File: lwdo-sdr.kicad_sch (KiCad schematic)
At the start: 21 parts, among them J101 IN1, J102 IN2, J103 IN3, J104 IN4, J105 USB_B, J106 CLK_OUT, J107 REF_IN

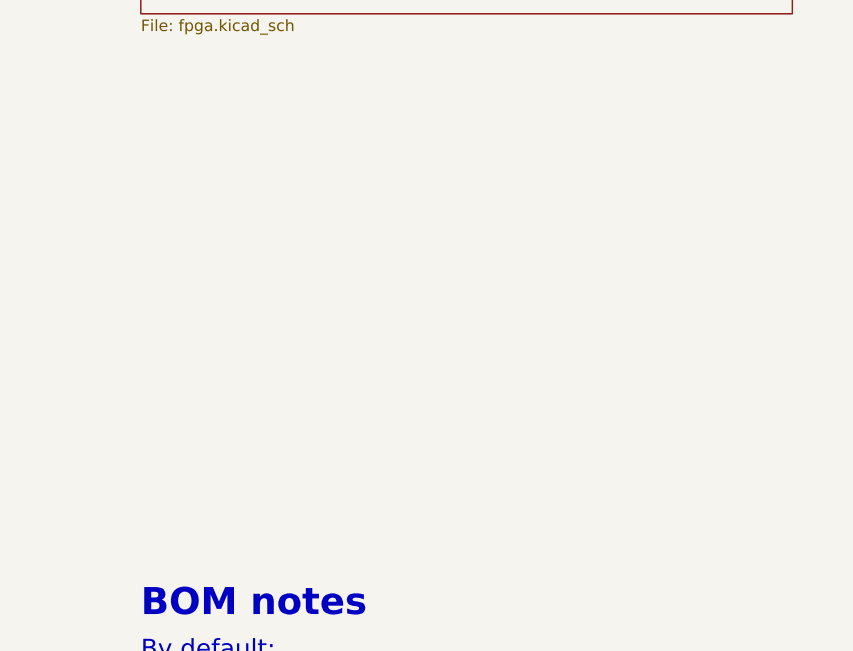
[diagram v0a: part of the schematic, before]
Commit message: Schematic: add mounting holes
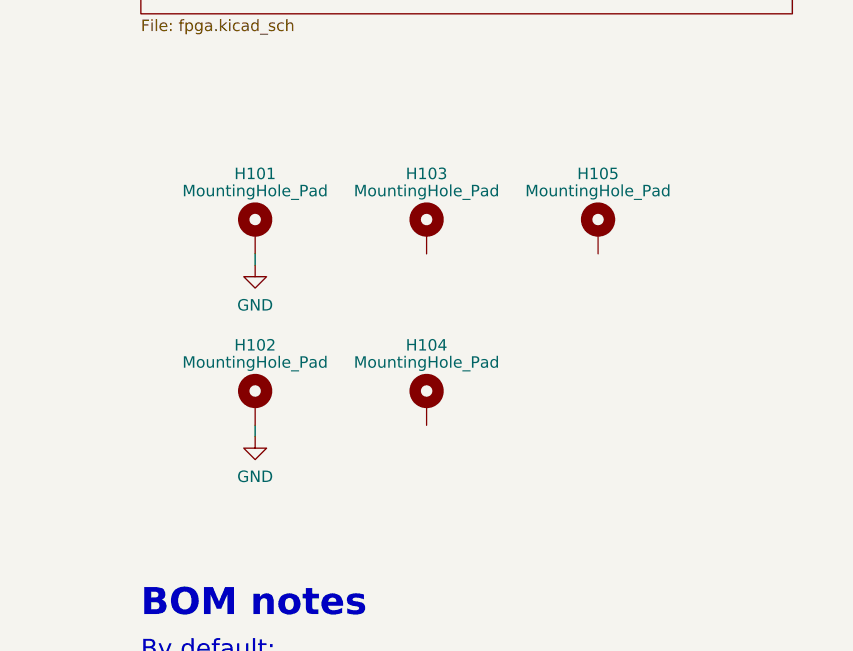
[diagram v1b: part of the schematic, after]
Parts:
- added H101, H102, H103, H104, H105: MountingHole_Pad, MountingHole:MountingHole_3.2mm_M3_Pad, symbol Mechanical:MountingHole_Pad
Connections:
- net GND: now also H101.1, H102.1
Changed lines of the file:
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@@
+    (stroke (width 0) (type default) (color 0 0 0 0))
+  )
+  (wire (pts (xy 215.9 187.96) (xy 215.9 189.23))
     (stroke (width 0) (type default) (color 0 0 0 0))
   )
@@
   )
   (wire (pts (xy 121.92 125.73) (xy 121.92 107.95))
+    (stroke (width 0) (type default) (color 0 0 0 0))
+  )
+  (wire (pts (xy 215.9 168.91) (xy 215.9 170.18))
     (stroke (width 0) (type default) (color 0 0 0 0))
   )
@@
     )
     (property "Datasheet" "" (id 3) (at 63.5 82.55 0)
+      (effects (font (size 1.27 1.27)) hide)
+    )
+    (pin "1")
+  )
+  (symbol (lib_id "Mechanical:MountingHole_Pad") (at 234.95 185.42 0) (unit 1)
+    (in_bom yes) (on_board yes) (fields_autoplaced)
+    (property "Reference" "H104" (id 0) (at 234.95 179.07 0))
+    (property "Value" "MountingHole_Pad" (id 1) (at 234.95 180.975 0))
+    (property "Footprint" "MountingHole:MountingHole_3.2mm_M3_Pad" (id 2) (at 234.95 185.42 0)
+      (effects (font (size 1.27 1.27)) hide)
+    )
+    (property "Datasheet" "~" (id 3) (at 234.95 185.42 0)
       (effects (font (size 1.27 1.27)) hide)
     )
@@
     (pin "1")
   )
+  (symbol (lib_id "power:GND") (at 215.9 189.23 0) (unit 1)
+    (in_bom yes) (on_board yes) (fields_autoplaced)
+    (property "Reference" "#PWR0121" (id 0) (at 215.9 195.58 0)
+      (effects (font (size 1.27 1.27)) hide)
+    )
+    (property "Value" "GND" (id 1) (at 215.9 193.6734 0))
+    (property "Footprint" "" (id 2) (at 215.9 189.23 0)
+      (effects (font (size 1.27 1.27)) hide)
+    )
+    (property "Datasheet" "" (id 3) (at 215.9 189.23 0)
+      (effects (font (size 1.27 1.27)) hide)
+    )
+    (pin "1")
+  )
   (symbol (lib_id "Connector:Conn_Coaxial") (at 63.5 76.2 0) (mirror y) (unit 1)
     (in_bom yes) (on_board yes) (fields_autoplaced)
@@
     (pin "1")
     (pin "2")
+  )
+  (symbol (lib_id "Mechanical:MountingHole_Pad") (at 254 166.37 0) (unit 1)
+    (in_bom yes) (on_board yes) (fields_autoplaced)
+    (property "Reference" "H105" (id 0) (at 254 160.02 0))
+    (property "Value" "MountingHole_Pad" (id 1) (at 254 161.925 0))
+    (property "Footprint" "MountingHole:MountingHole_3.2mm_M3_Pad" (id 2) (at 254 166.37 0)
+      (effects (font (size 1.27 1.27)) hide)
+    )
+    (property "Datasheet" "~" (id 3) (at 254 166.37 0)
+      (effects (font (size 1.27 1.27)) hide)
+    )
+    (pin "1")
   )
   (symbol (lib_id "power:GND") (at 379.73 179.07 0) (mirror y) (unit 1)
@@
     (pin "1")
   )
+  (symbol (lib_id "Mechanical:MountingHole_Pad") (at 215.9 166.37 0) (unit 1)
+    (in_bom yes) (on_board yes) (fields_autoplaced)
+    (property "Reference" "H101" (id 0) (at 215.9 160.02 0))
+    (property "Value" "MountingHole_Pad" (id 1) (at 215.9 161.925 0))
+    (property "Footprint" "MountingHole:MountingHole_3.2mm_M3_Pad" (id 2) (at 215.9 166.37 0)
+      (effects (font (size 1.27 1.27)) hide)
+    )
+    (property "Datasheet" "~" (id 3) (at 215.9 166.37 0)
+      (effects (font (size 1.27 1.27)) hide)
+    )
+    (pin "1")
+  )
   (symbol (lib_id "Device:R") (at 355.6 180.34 90) (mirror x) (unit 1)
     (in_bom yes) (on_board yes) (fields_autoplaced)
@@
     (pin "1")
     (pin "2")
+  )
+  (symbol (lib_id "power:GND") (at 215.9 170.18 0) (unit 1)
+    (in_bom yes) (on_board yes) (fields_autoplaced)
+    (property "Reference" "#PWR0123" (id 0) (at 215.9 176.53 0)
+      (effects (font (size 1.27 1.27)) hide)
+    )
+    (property "Value" "GND" (id 1) (at 215.9 174.6234 0))
+    (property "Footprint" "" (id 2) (at 215.9 170.18 0)
+      (effects (font (size 1.27 1.27)) hide)
+    )
+    (property "Datasheet" "" (id 3) (at 215.9 170.18 0)
+      (effects (font (size 1.27 1.27)) hide)
+    )
+    (pin "1")
   )
   (symbol (lib_id "symbols:WP130WCP{slash}2EGW") (at 369.57 228.6 0) (mirror y) (unit 2)
@@
     (pin "1")
   )
+  (symbol (lib_id "Mechanical:MountingHole_Pad") (at 234.95 166.37 0) (unit 1)
+    (in_bom yes) (on_board yes) (fields_autoplaced)
+    (property "Reference" "H103" (id 0) (at 234.95 160.02 0))
+    (property "Value" "MountingHole_Pad" (id 1) (at 234.95 161.925 0))
+    (property "Footprint" "MountingHole:MountingHole_3.2mm_M3_Pad" (id 2) (at 234.95 166.37 0)
+      (effects (font (size 1.27 1.27)) hide)
+    )
+    (property "Datasheet" "~" (id 3) (at 234.95 166.37 0)
+      (effects (font (size 1.27 1.27)) hide)
+    )
+    (pin "1")
+  )
   (symbol (lib_id "Connector:Conn_Coaxial") (at 63.5 101.6 0) (mirror y) (unit 1)
     (in_bom yes) (on_board yes) (fields_autoplaced)
@@
     )
     (property "Datasheet" "" (id 3) (at 379.73 204.47 0)
+      (effects (font (size 1.27 1.27)) hide)
+    )
+    (pin "1")
+  )
+  (symbol (lib_id "Mechanical:MountingHole_Pad") (at 215.9 185.42 0) (unit 1)
+    (in_bom yes) (on_board yes) (fields_autoplaced)
+    (property "Reference" "H102" (id 0) (at 215.9 179.07 0))
+    (property "Value" "MountingHole_Pad" (id 1) (at 215.9 180.975 0))
+    (property "Footprint" "MountingHole:MountingHole_3.2mm_M3_Pad" (id 2) (at 215.9 185.42 0)
+      (effects (font (size 1.27 1.27)) hide)
+    )
+    (property "Datasheet" "~" (id 3) (at 215.9 185.42 0)
       (effects (font (size 1.27 1.27)) hide)
     )
@@
       (reference "#PWR0119") (unit 1) (value "GND") (footprint "")
     )
+    (path "/19a8867c-b5b9-40de-b8d0-7d57e00cda38"
+      (reference "#PWR0121") (unit 1) (value "GND") (footprint "")
+    )
+    (path "/7816e58c-df5c-4478-a780-33cfa46d1a5a"
+      (reference "#PWR0123") (unit 1) (value "GND") (footprint "")
+    )
     (path "/d26f84ce-09cf-42fc-96be-2f9ccec4a29a/d5ee710c-195c-4609-b9c4-8543f1d16063"
       (reference "#PWR0201") (unit 1) (value "+3.3VD") (footprint "")
@@
       (reference "FB1401") (unit 1) (value "782853701") (footprint "Inductor_SMD:L_0805_2012Metric_Pad1.05x1.20mm_HandSolder")
     )
+    (path "/75926d66-4335-4a1d-90b5-2048e56449d0"
+      (reference "H101") (unit 1) (value "MountingHole_Pad") (footprint "MountingHole:MountingHole_3.2mm_M3_Pad")
+    )
+    (path "/c333556c-d248-41ae-9e09-f36eb84a6b0d"
+      (reference "H102") (unit 1) (value "MountingHole_Pad") (footprint "MountingHole:MountingHole_3.2mm_M3_Pad")
+    )
+    (path "/b50d6abc-7e81-417f-b08e-74be30f4cfd0"
+      (reference "H103") (unit 1) (value "MountingHole_Pad") (footprint "MountingHole:MountingHole_3.2mm_M3_Pad")
+    )
+    (path "/0169c51d-a64d-4c21-8122-4c6a2fb8b4ab"
+      (reference "H104") (unit 1) (value "MountingHole_Pad") (footprint "MountingHole:MountingHole_3.2mm_M3_Pad")
+    )
+    (path "/24b7e51e-7b6f-4e07-a7fe-70a6f1d77734"
+      (reference "H105") (unit 1) (value "MountingHole_Pad") (footprint "MountingHole:MountingHole_3.2mm_M3_Pad")
+    )
     (path "/4237216f-1980-4d4e-a9e0-4008f7caeeed"

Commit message: Add and use Superbat SMA connector footprint
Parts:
- J101, J102, J103, J104, J106, J107: footprint Connector_Coaxial:SMA_Molex_73251-2200_Horizontal -> custom-footprints:SMA_Superbat_S01-ROPT4-11BS00
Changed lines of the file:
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@@
     (property "Reference" "J104" (id 0) (at 63.8174 121.4736 0))
     (property "Value" "IN4" (id 1) (at 63.8174 124.0105 0))
-    (property "Footprint" "Connector_Coaxial:SMA_Molex_73251-2200_Horizontal" (id 2) (at 63.5 127 0)
+    (property "Footprint" "custom-footprints:SMA_Superbat_S01-ROPT4-11BS00" (id 2) (at 63.5 127 0)
       (effects (font (size 1.27 1.27)) hide)
     )
@@
     (property "Reference" "J102" (id 0) (at 63.8174 70.6736 0))
     (property "Value" "IN2" (id 1) (at 63.8174 73.2105 0))
-    (property "Footprint" "Connector_Coaxial:SMA_Molex_73251-2200_Horizontal" (id 2) (at 63.5 76.2 0)
+    (property "Footprint" "custom-footprints:SMA_Superbat_S01-ROPT4-11BS00" (id 2) (at 63.5 76.2 0)
       (effects (font (size 1.27 1.27)) hide)
     )
@@
     (property "Reference" "J101" (id 0) (at 63.8174 45.2736 0))
     (property "Value" "IN1" (id 1) (at 63.8174 47.8105 0))
-    (property "Footprint" "Connector_Coaxial:SMA_Molex_73251-2200_Horizontal" (id 2) (at 63.5 50.8 0)
+    (property "Footprint" "custom-footprints:SMA_Superbat_S01-ROPT4-11BS00" (id 2) (at 63.5 50.8 0)
       (effects (font (size 1.27 1.27)) hide)
     )
@@
       (effects (font (size 1.27 1.27)) (justify left))
     )
-    (property "Footprint" "Connector_Coaxial:SMA_Molex_73251-2200_Horizontal" (id 2) (at 342.9 101.6 0)
+    (property "Footprint" "custom-footprints:SMA_Superbat_S01-ROPT4-11BS00" (id 2) (at 342.9 101.6 0)
       (effects (font (size 1.27 1.27)) hide)
     )
@@
       (effects (font (size 1.27 1.27)) (justify left))
     )
-    (property "Footprint" "Connector_Coaxial:SMA_Molex_73251-2200_Horizontal" (id 2) (at 342.9 62.23 0)
+    (property "Footprint" "custom-footprints:SMA_Superbat_S01-ROPT4-11BS00" (id 2) (at 342.9 62.23 0)
       (effects (font (size 1.27 1.27)) hide)
     )
@@
     (property "Reference" "J103" (id 0) (at 63.8174 96.0736 0))
     (property "Value" "IN3" (id 1) (at 63.8174 98.6105 0))
-    (property "Footprint" "Connector_Coaxial:SMA_Molex_73251-2200_Horizontal" (id 2) (at 63.5 101.6 0)
+    (property "Footprint" "custom-footprints:SMA_Superbat_S01-ROPT4-11BS00" (id 2) (at 63.5 101.6 0)
       (effects (font (size 1.27 1.27)) hide)
     )
@@
     )
     (path "/4237216f-1980-4d4e-a9e0-4008f7caeeed"
-      (reference "J101") (unit 1) (value "IN1") (footprint "Connector_Coaxial:SMA_Molex_73251-2200_Horizontal")
+      (reference "J101") (unit 1) (value "IN1") (footprint "custom-footprints:SMA_Superbat_S01-ROPT4-11BS00")
     )
     (path "/215be0a7-153a-4e22-aec6-8d9afc1b371d"
-      (reference "J102") (unit 1) (value "IN2") (footprint "Connector_Coaxial:SMA_Molex_73251-2200_Horizontal")
+      (reference "J102") (unit 1) (value "IN2") (footprint "custom-footprints:SMA_Superbat_S01-ROPT4-11BS00")
     )
     (path "/bbe93777-151a-4b3d-85c8-52f7d82c6ac1"
-      (reference "J103") (unit 1) (value "IN3") (footprint "Connector_Coaxial:SMA_Molex_73251-2200_Horizontal")
+      (reference "J103") (unit 1) (value "IN3") (footprint "custom-footprints:SMA_Superbat_S01-ROPT4-11BS00")
     )
     (path "/10de0316-f50c-41bc-b1a7-9e2ead88633d"
-      (reference "J104") (unit 1) (value "IN4") (footprint "Connector_Coaxial:SMA_Molex_73251-2200_Horizontal")
+      (reference "J104") (unit 1) (value "IN4") (footprint "custom-footprints:SMA_Superbat_S01-ROPT4-11BS00")
     )
     (path "/11335b39-a06a-4687-a18f-a62cc5f4c31e"
@@
     )
     (path "/a3049626-42e2-4901-9209-abf8037b2db1"
-      (reference "J106") (unit 1) (value "CLK_OUT") (footprint "Connector_Coaxial:SMA_Molex_73251-2200_Horizontal")
+      (reference "J106") (unit 1) (value "CLK_OUT") (footprint "custom-footprints:SMA_Superbat_S01-ROPT4-11BS00")
     )
     (path "/6bf68021-b6d9-4b68-b5d0-e7bba7266a3a"
-      (reference "J107") (unit 1) (value "REF_IN") (footprint "Connector_Coaxial:SMA_Molex_73251-2200_Horizontal")
+      (reference "J107") (unit 1) (value "REF_IN") (footprint "custom-footprints:SMA_Superbat_S01-ROPT4-11BS00")
     )
     (path "/6c944c46-64bf-4c4b-bb86-1cfbfa0c92c2/0805070c-2ea9-411a-9750-9cdf6d83d8cc"

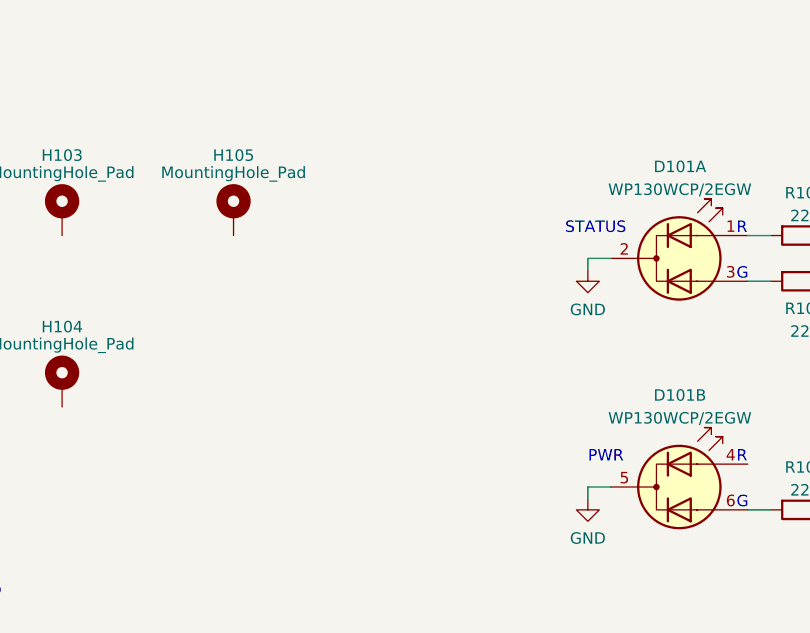
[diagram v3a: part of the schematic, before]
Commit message: Add two GND testpoints to the schematic
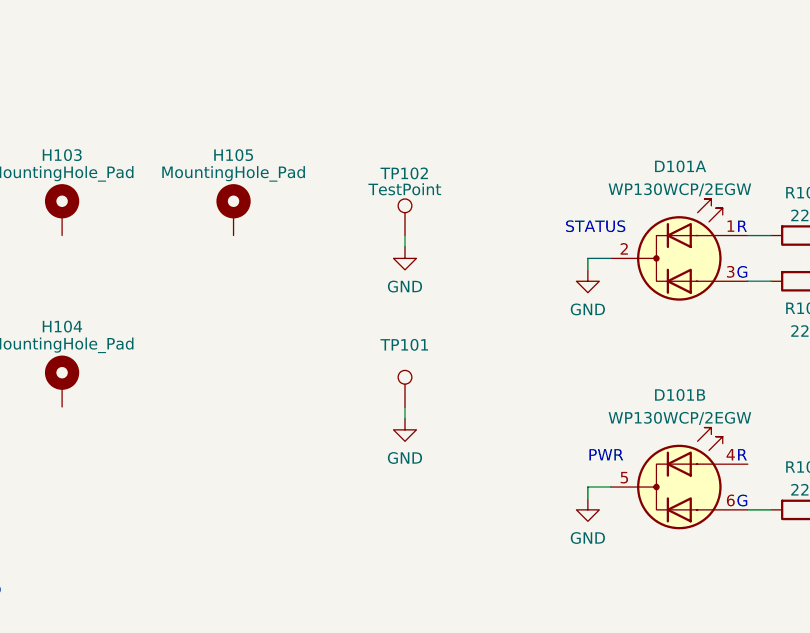
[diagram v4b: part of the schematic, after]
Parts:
- added TP101: (no value), symbol Connector:TestPoint
- added TP102: TestPoint, TestPoint:TestPoint_Bridge_Pitch5.08mm_Drill1.3mm, symbol Connector:TestPoint
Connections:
- net GND: now also TP101.1, TP102.1
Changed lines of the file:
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@@
     (stroke (width 0) (type default) (color 0 0 0 0))
   )
+  (wire (pts (xy 273.05 168.91) (xy 273.05 170.18))
+    (stroke (width 0) (type default) (color 0 0 0 0))
+  )
   (wire (pts (xy 379.73 152.4) (xy 377.19 152.4))
     (stroke (width 0) (type default) (color 0 0 0 0))
@@
     (stroke (width 0) (type default) (color 0 0 0 0))
   )
+  (wire (pts (xy 273.05 187.96) (xy 273.05 189.23))
+    (stroke (width 0) (type default) (color 0 0 0 0))
+  )
   (wire (pts (xy 115.57 125.73) (xy 121.92 125.73))
     (stroke (width 0) (type default) (color 0 0 0 0))
@@
     (pin "1")
   )
+  (symbol (lib_id "power:GND") (at 273.05 189.23 0) (unit 1)
+    (in_bom yes) (on_board yes) (fields_autoplaced)
+    (property "Reference" "#PWR0120" (id 0) (at 273.05 195.58 0)
+      (effects (font (size 1.27 1.27)) hide)
+    )
+    (property "Value" "GND" (id 1) (at 273.05 193.6734 0))
+    (property "Footprint" "" (id 2) (at 273.05 189.23 0)
+      (effects (font (size 1.27 1.27)) hide)
+    )
+    (property "Datasheet" "" (id 3) (at 273.05 189.23 0)
+      (effects (font (size 1.27 1.27)) hide)
+    )
+    (pin "1")
+  )
   (symbol (lib_id "power:GND") (at 342.9 107.95 0) (unit 1)
     (in_bom yes) (on_board yes) (fields_autoplaced)
@@
     (pin "2")
   )
+  (symbol (lib_id "power:GND") (at 273.05 170.18 0) (unit 1)
+    (in_bom yes) (on_board yes) (fields_autoplaced)
+    (property "Reference" "#PWR0122" (id 0) (at 273.05 176.53 0)
+      (effects (font (size 1.27 1.27)) hide)
+    )
+    (property "Value" "GND" (id 1) (at 273.05 174.6234 0))
+    (property "Footprint" "" (id 2) (at 273.05 170.18 0)
+      (effects (font (size 1.27 1.27)) hide)
+    )
+    (property "Datasheet" "" (id 3) (at 273.05 170.18 0)
+      (effects (font (size 1.27 1.27)) hide)
+    )
+    (pin "1")
+  )
   (symbol (lib_id "Device:R") (at 317.5 168.91 270) (unit 1)
     (in_bom yes) (on_board yes) (fields_autoplaced)
@@
     (pin "2")
   )
+  (symbol (lib_id "Connector:TestPoint") (at 273.05 168.91 0) (unit 1)
+    (in_bom yes) (on_board yes)
+    (property "Reference" "TP102" (id 0) (at 273.05 162.052 0))
+    (property "Value" "TestPoint" (id 1) (at 273.05 163.83 0))
+    (property "Footprint" "TestPoint:TestPoint_Bridge_Pitch5.08mm_Drill1.3mm" (id 2) (at 278.13 168.91 0)
+      (effects (font (size 1.27 1.27)) hide)
+    )
+    (property "Datasheet" "~" (id 3) (at 278.13 168.91 0)
+      (effects (font (size 1.27 1.27)) hide)
+    )
+    (pin "1")
+  )
   (symbol (lib_id "power:GND") (at 379.73 229.87 0) (mirror y) (unit 1)
     (in_bom yes) (on_board yes) (fields_autoplaced)
@@
     (pin "2")
   )
+  (symbol (lib_id "Connector:TestPoint") (at 273.05 187.96 0) (unit 1)
+    (in_bom yes) (on_board yes)
+    (property "Reference" "TP101" (id 0) (at 273.05 181.102 0))
+    (property "Value" "" (id 1) (at 273.05 182.88 0))
+    (property "Footprint" "" (id 2) (at 278.13 187.96 0)
+      (effects (font (size 1.27 1.27)) hide)
+    )
+    (property "Datasheet" "~" (id 3) (at 278.13 187.96 0)
+      (effects (font (size 1.27 1.27)) hide)
+    )
+    (pin "1")
+  )
   (symbol (lib_id "Device:R") (at 355.6 154.94 90) (mirror x) (unit 1)
     (in_bom yes) (on_board yes) (fields_autoplaced)
@@
       (reference "#PWR0119") (unit 1) (value "GND") (footprint "")
     )
+    (path "/0a7a71df-c15e-4333-a328-3448ff95e024"
+      (reference "#PWR0120") (unit 1) (value "GND") (footprint "")
+    )
     (path "/19a8867c-b5b9-40de-b8d0-7d57e00cda38"
       (reference "#PWR0121") (unit 1) (value "GND") (footprint "")
     )
+    (path "/4fd469f8-4000-4124-9512-7af85bbdb5f3"
+      (reference "#PWR0122") (unit 1) (value "GND") (footprint "")
+    )
     (path "/7816e58c-df5c-4478-a780-33cfa46d1a5a"
       (reference "#PWR0123") (unit 1) (value "GND") (footprint "")
@@
       (reference "RN1404") (unit 1) (value "4x82R") (footprint "Resistor_SMD:R_Array_Convex_4x0603")
     )
+    (path "/d4cb3dc0-269e-472d-be6c-8159acadb537"
+      (reference "TP101") (unit 1) (value "TestPoint") (footprint "TestPoint:TestPoint_Bridge_Pitch5.08mm_Drill1.3mm")
+    )
+    (path "/a8dae3a6-f54a-4dc2-827b-70f2d4a70924"
+      (reference "TP102") (unit 1) (value "TestPoint") (footprint "TestPoint:TestPoint_Bridge_Pitch5.08mm_Drill1.3mm")
+    )
     (path "/ce49f942-6156-4865-828b-a40f6feba933/2da3bf0c-1690-48da-88ef-39dd060179b6"
